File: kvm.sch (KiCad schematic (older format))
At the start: 16 parts, among them J0 USB_C_Receptacle, J1 USB_C_Receptacle, J2 USB_C_Receptacle, U0 HD3SS3212, U1 HD3SS3212, U2 HD3SS3212

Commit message: Added a micro controller and SWD header
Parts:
- removed C?: ?F, symbol Device:C
- removed C? (x2): 1uF, symbol Device:C
- removed D1, D2, D3: D_Schottky, Diode_SMD:D_SOD-123, symbol Device:D_Schottky
- removed R0: 56k, Resistor_SMD:R_0805_2012Metric_Pad1.20x1.40mm_HandSolder, symbol Device:R
- removed R?: 10k, symbol Device:R
- removed U?: MAX17501AxTB, Package_DFN_QFN:TDFN-10-1EP_2x3mm_P0.5mm_EP0.9x2mm, symbol Regulator_Switching:MAX17501AxTB
- added C1, C2: 30p, Capacitor_SMD:C_0805_2012Metric, symbol Device:C
- added J3: Conn_ARM_JTAG_SWD_10, Connector_PinHeader_1.27mm:PinHeader_2x05_P1.27mm_Vertical_SMD, symbol Connector:Conn_ARM_JTAG_SWD_10
- added R2: 10k, Resistor_SMD:R_0805_2012Metric, symbol Device:R
- added SW1: SW_Push, Button_Switch_SMD:SW_SPST_B3S-1000, symbol Switch:SW_Push
- added U3: STM32F030F4Px, Package_SO:TSSOP-20_4.4x6.5mm_P0.65mm, symbol MCU_ST_STM32F0:STM32F030F4Px
- added Y1: Crystal, Crystal:Crystal_HC49-4H_Vertical, symbol Device:Crystal
- J0: footprint Connector_USB:USB_C_Receptacle_GCT_USB4085 -> Connector_USB:USB_C_Receptacle_Amphenol_12401548E4-2A
- J1: renamed from J2; footprint Connector_USB:USB_C_Receptacle_GCT_USB4085 -> Connector_USB:USB_C_Receptacle_Amphenol_12401548E4-2A
- J2: renamed from J1; footprint Connector_USB:USB_C_Receptacle_GCT_USB4085 -> Connector_USB:USB_C_Receptacle_Amphenol_12401548E4-2A
- R1: value 56k -> 10k; footprint Resistor_SMD:R_0805_2012Metric_Pad1.20x1.40mm_HandSolder -> Resistor_SMD:R_0805_2012Metric
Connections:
- net labels added: CRY0, CRY1, I1D+, I1D-, I1RX1+, I1RX1-, I1RX2+, I1RX2-, I1SBU1, I1SBU2, I1TX1+, I1TX1-, I1TX2+, I1TX2-, I2D+, I2D-, I2RX1+, I2RX1-, I2RX2+, I2RX2-, I2SBU1, I2SBU2, I2TX1+, I2TX1-, I2TX2+, I2TX2-, NRST, OD+, OD-, ORX1+, ORX1-, ORX2+, ORX2-, OSBU1, OSBU2, OTX1+, OTX1-, OTX2+, OTX2-, SWCLK, SWDIO
- wire segments 148 -> 126
- no-connect marks 7 -> 15
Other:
- moved on the sheet: J0, J1, J2, U0, U1, U2

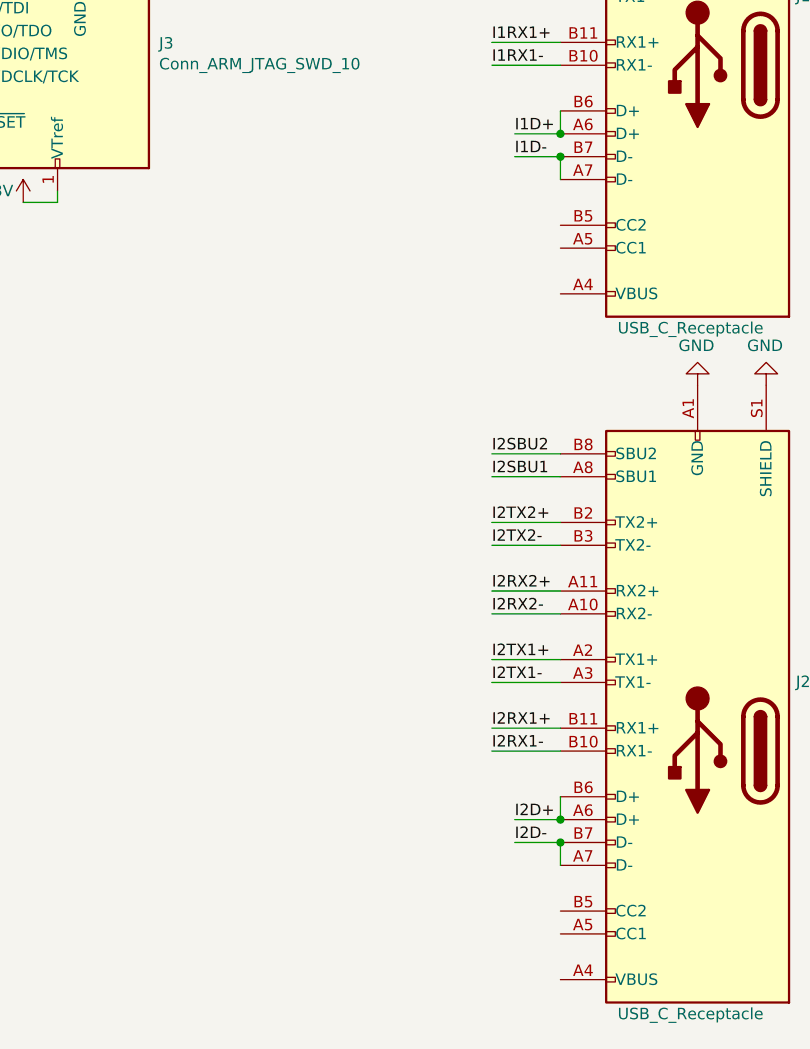
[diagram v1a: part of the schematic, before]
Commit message: Added a power buffer on VBus
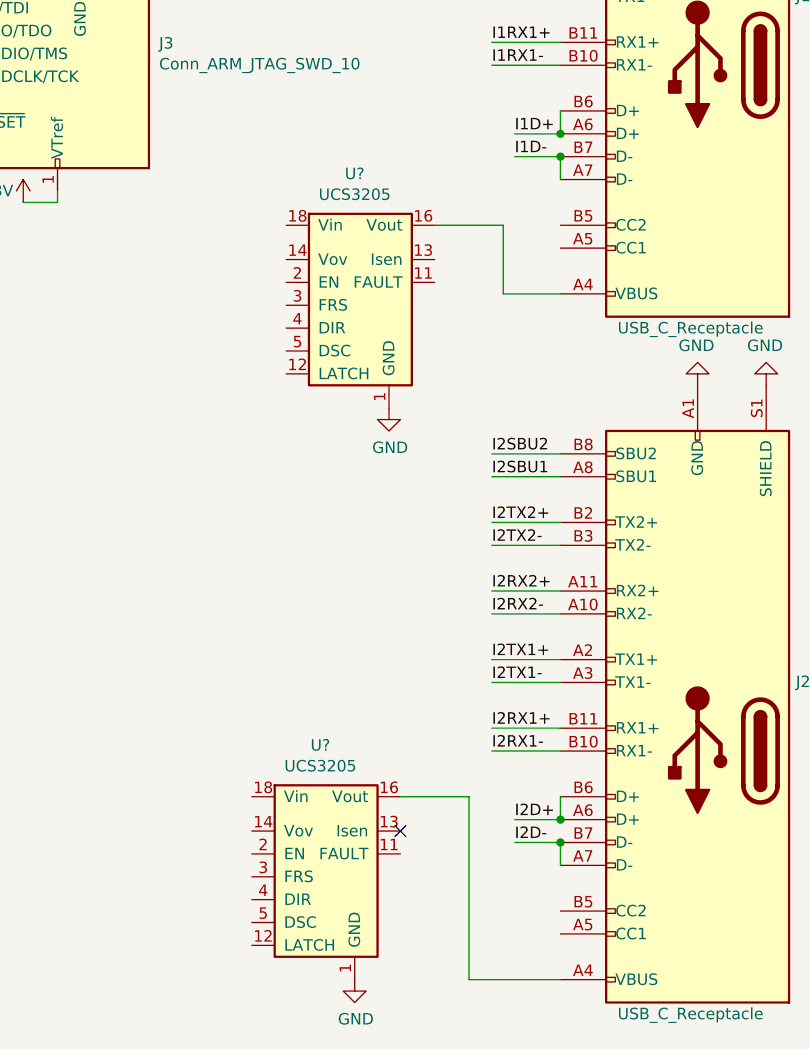
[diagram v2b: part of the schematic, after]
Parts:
- added U? (x2): UCS3205, symbol vendor:UCS3205
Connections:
- net GND: now also U?.1 (GND), U?.1 (GND), U?.15 (GND), U?.15 (GND)
- net at J1.A4 (VBUS), J1.A9 (VBUS), J1.B4 (VBUS)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: now also U?.16 (Vout), U?.17 (Vout), U?.21 (Vout)
- net at J2.A4 (VBUS), J2.A9 (VBUS), J2.B4 (VBUS)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: now also U?.16 (Vout), U?.17 (Vout), U?.21 (Vout)
- new net: U?.18 (Vin), U?.19 (Vin), U?.20 (Vin) (x2)
- no-connect marks 15 -> 16
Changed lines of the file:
@@
 Text Label 5700 2150 0    50   ~ 0
 CRY1
+$Comp
+L vendor:UCS3205 U?
+U 1 1 60CE04F3
+P 9200 3400
+F 0 "U?" H 9200 4025 50  0000 C CNN
+F 1 "UCS3205" H 9200 3934 50  0000 C CNN
+F 2 "" H 9550 3950 50  0001 C CNN
+F 3 "https://www.mouser.co.uk/datasheet/2/268/UCS3205_Data_Sheet_DS20006433A-1915299.pdf" H 9600 3950 50  0001 C CNN
+	1    9200 3400
+	1    0    0    -1
+$EndComp
+$Comp
+L power:GND #PWR?
+U 1 1 60CF5D7A
+P 9350 3800
+F 0 "#PWR?" H 9350 3550 50  0001 C CNN
+F 1 "GND" H 9355 3627 50  0000 C CNN
+F 2 "" H 9350 3800 50  0001 C CNN
+F 3 "" H 9350 3800 50  0001 C CNN
+	1    9350 3800
+	1    0    0    -1
+$EndComp
+Wire Wire Line
+	9550 3000 9850 3000
+Wire Wire Line
+	9850 3000 9850 3300
+Wire Wire Line
+	9850 3300 10100 3300
+$Comp
+L vendor:UCS3205 U?
+U 1 1 60D16145
+P 9050 5900
+F 0 "U?" H 9050 6525 50  0000 C CNN
+F 1 "UCS3205" H 9050 6434 50  0000 C CNN
+F 2 "" H 9400 6450 50  0001 C CNN
+F 3 "https://www.mouser.co.uk/datasheet/2/268/UCS3205_Data_Sheet_DS20006433A-1915299.pdf" H 9450 6450 50  0001 C CNN
+	1    9050 5900
+	1    0    0    -1
+$EndComp
+$Comp
+L power:GND #PWR?
+U 1 1 60D1614B
+P 9200 6300
+F 0 "#PWR?" H 9200 6050 50  0001 C CNN
+F 1 "GND" H 9205 6127 50  0000 C CNN
+F 2 "" H 9200 6300 50  0001 C CNN
+F 3 "" H 9200 6300 50  0001 C CNN
+	1    9200 6300
+	1    0    0    -1
+$EndComp
+Wire Wire Line
+	9400 5500 9700 5500
+Wire Wire Line
+	9700 5500 9700 6300
+Wire Wire Line
+	9700 6300 10100 6300
+NoConn ~ 9400 5650
 $EndSCHEMATC

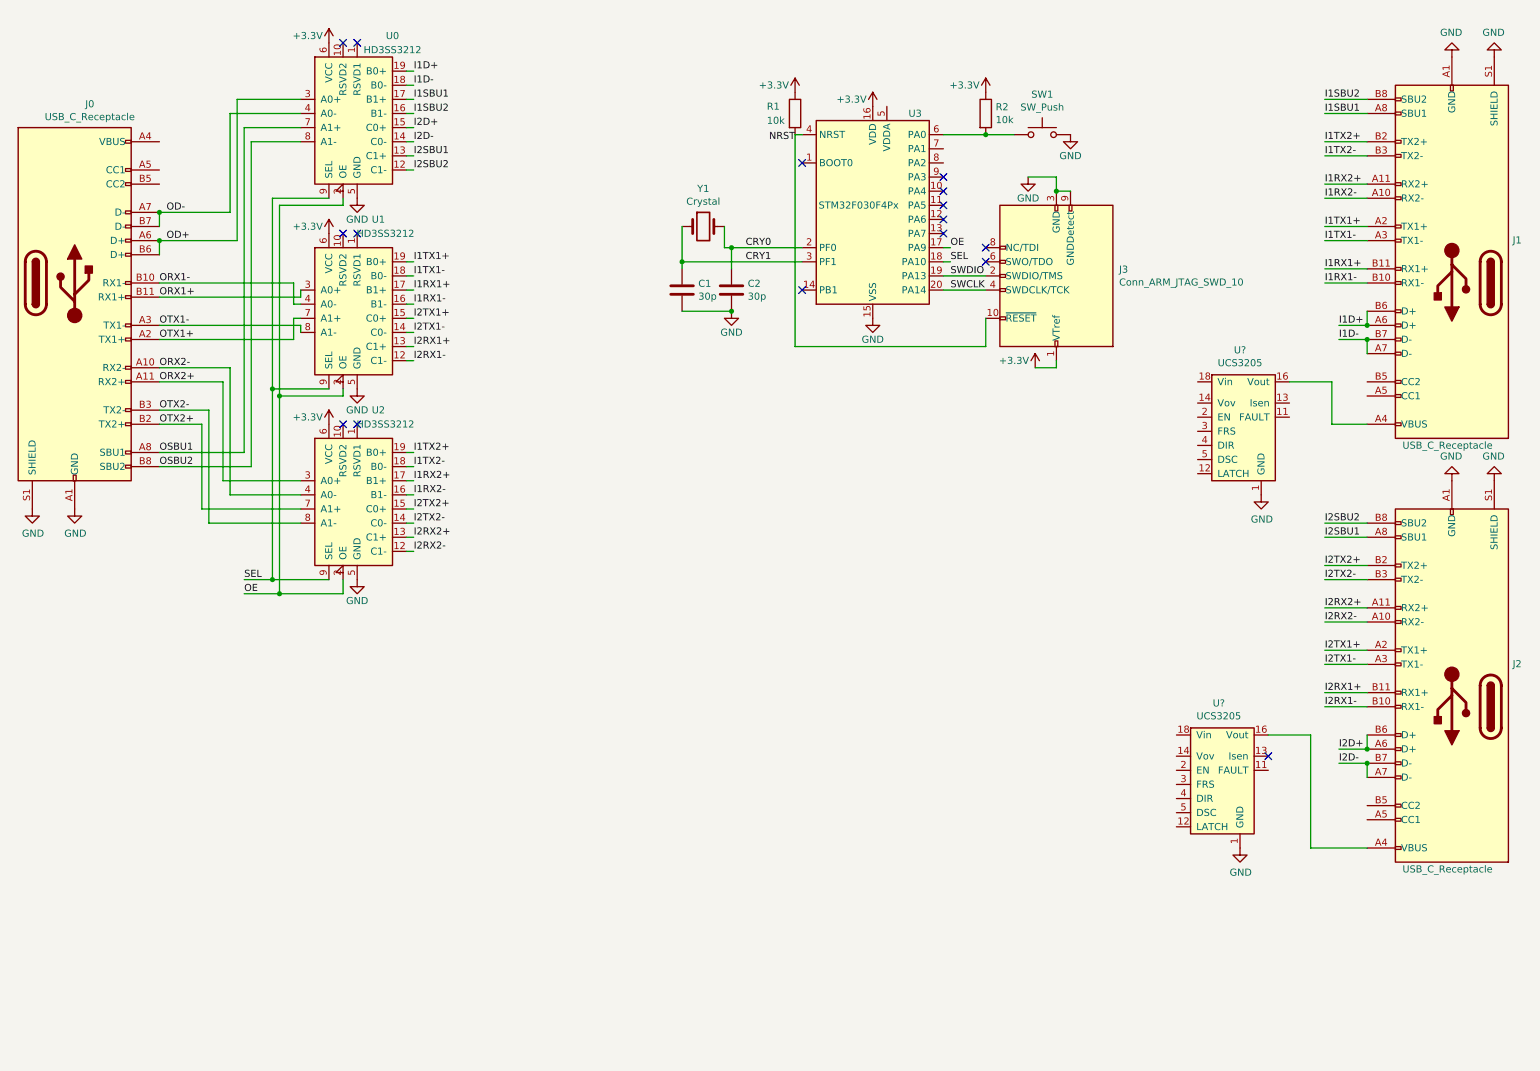
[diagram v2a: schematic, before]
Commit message: finished PD switches and added 3.3V PSU
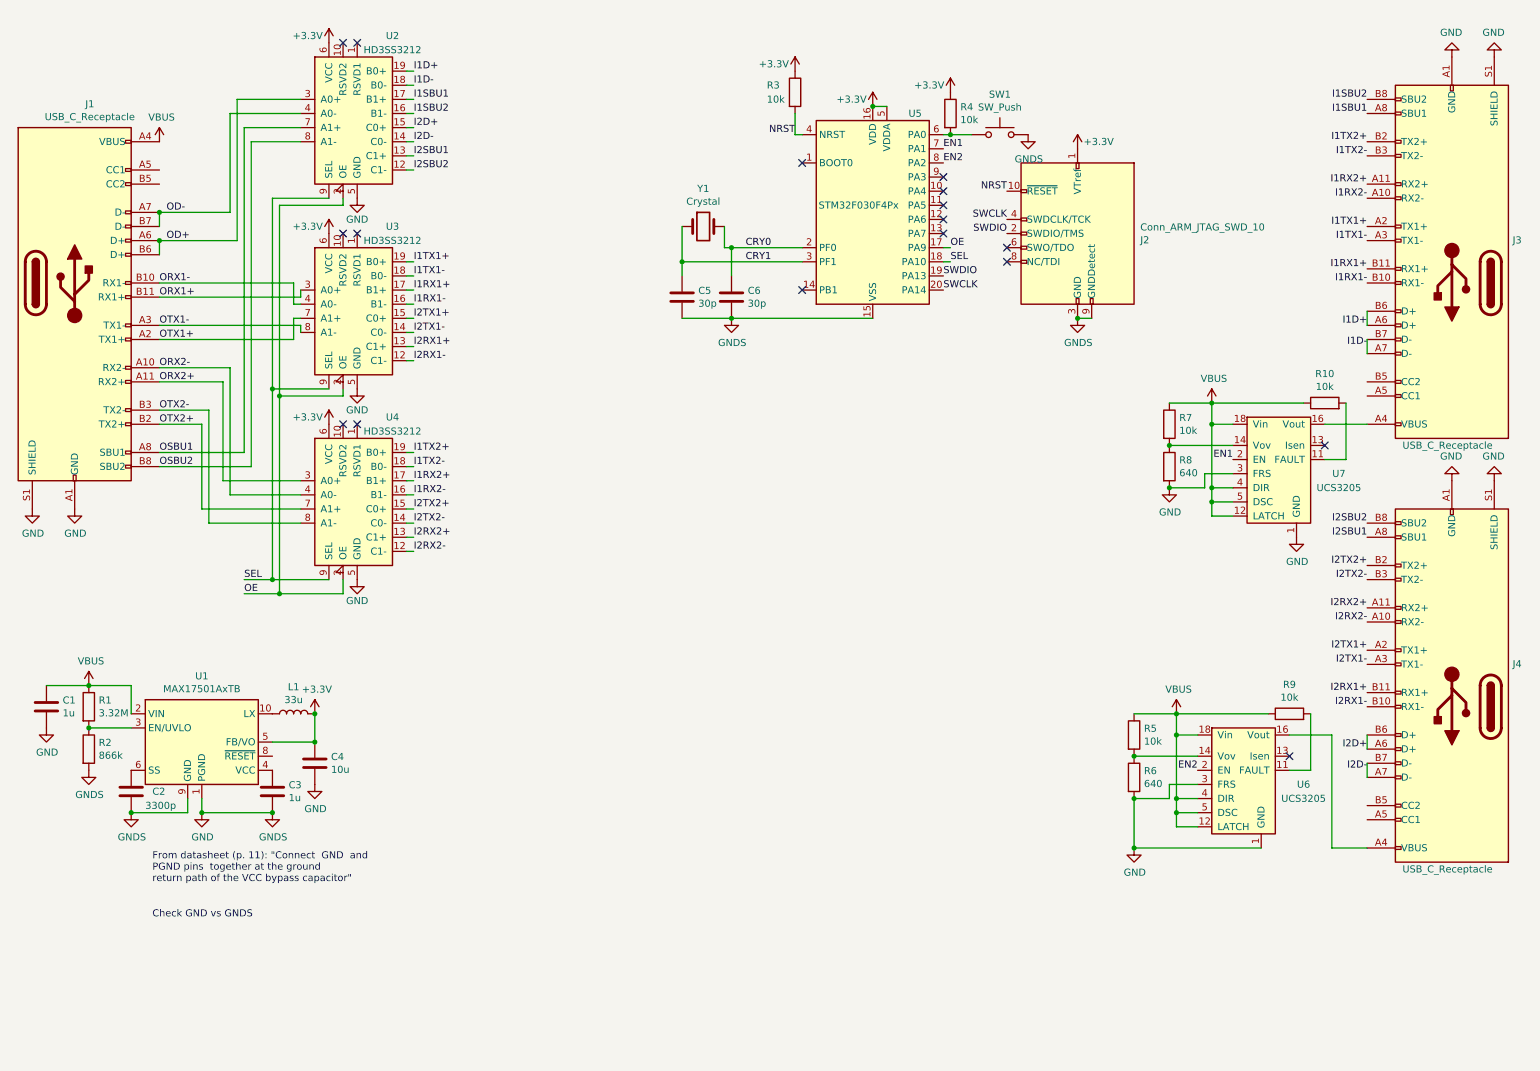
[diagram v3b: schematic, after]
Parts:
- removed U?: UCS3205, symbol vendor:UCS3205
- added C1, C3: 1u, Capacitor_SMD:C_0805_2012Metric, symbol Device:C
- added C2: 3300p, Capacitor_SMD:C_0805_2012Metric, symbol Device:C
- added C4: 10u, Capacitor_SMD:C_1206_3216Metric, symbol Device:C
- added L1: 33u, Inductor_SMD:L_0805_2012Metric, symbol Device:L
- added R1: 3.32M, Resistor_SMD:R_0805_2012Metric, symbol Device:R
- added R10, R5, R7, R9: 10k, Resistor_SMD:R_0805_2012Metric, symbol Device:R
- added R2: 866k, Resistor_SMD:R_0805_2012Metric, symbol Device:R
- added R6, R8: 640, Resistor_SMD:R_0805_2012Metric, symbol Device:R
- added U1: MAX17501AxTB, Package_DFN_QFN:TDFN-10-1EP_2x3mm_P0.5mm_EP0.9x2mm, symbol Regulator_Switching:MAX17501AxTB
- added U7: UCS3205, VQFN20:VQFN19_3x3x0.9mm, symbol vendor:UCS3205
- U6: renamed from U?; footprint (none) -> VQFN20:VQFN19_3x3x0.9mm
- renumbered C1 to C5, C2 to C6, J0 to J1, J3 to J2, J1 to J3, J2 to J4, R1 to R3, R2 to R4, U0 to U2, U1 to U3, U2 to U4, U3 to U5
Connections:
- net +3V3: now also U5.5 (VDDA), C4.1, L1.2, U1.5 (FB/VO)
- net GND: now also U6.3 (FRS), C1.2, C2.2, C3.2, C4.2, R2.2, R6.2, R8.2, U1.1 (PGND), U1.11 (GND), U1.9 (GND), U7.1 (GND), U7.15 (GND), U7.3 (FRS)
- net VBUS: now reaches J1.A4 (VBUS), J1.A9 (VBUS), J1.B4 (VBUS), J1.B9 (VBUS)
- net VBUS: now also U6.12 (LATCH), U6.18 (Vin), U6.19 (Vin), U6.20 (Vin), U6.4 (DIR), U6.5 (DSC), C1.1, R1.1, R10.1, R5.1, R7.1, R9.1, U1.2 (VIN), U7.12 (LATCH), U7.18 (Vin), U7.19 (Vin), U7.20 (Vin), U7.4 (DIR), U7.5 (DSC)
- net at J3.A4 (VBUS), J3.A9 (VBUS), J3.B4 (VBUS)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: now also U7.16 (Vout), U7.17 (Vout), U7.21 (Vout)
- net EN1: now reaches U5.7 (PA1)
- net EN1: now also U7.2 (EN)
- net EN2: now reaches U5.8 (PA2)
- net EN2: now also U6.2 (EN)
- net at U6.11 (FAULT): now also R9.2
- net at U6.14 (Vov): now also R5.2, R6.1
- new net: R10.2, U7.11 (FAULT)
- new net: R7.2, R8.1, U7.14 (Vov)
- new net: L1.1, U1.10 (LX)
- new net: R1.2, R2.1, U1.3 (EN/UVLO)
- new net: C3.1, U1.4 (VCC)
- new net: C2.1, U1.6 (SS)
- no-connect marks 16 -> 17
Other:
- note added: "Check GND vs GNDS"
- note added: "From datasheet (p. 11): "Connect GND and \nPGND pins together at the ground\nreturn path of the VCC bypass capacitor""
- moved on the sheet: C5, C6, J2, R3, R4, SW1, U6

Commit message: Added PD, maybe finished v1!
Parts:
- removed C1, C3: 1u, Capacitor_SMD:C_0805_2012Metric, symbol Device:C
- removed C2: 3300p, Capacitor_SMD:C_0805_2012Metric, symbol Device:C
- removed C4: 10u, Capacitor_SMD:C_1206_3216Metric, symbol Device:C
- removed C5, C6: 30p, Capacitor_SMD:C_0805_2012Metric, symbol Device:C
- removed R1: 3.32M, Resistor_SMD:R_0805_2012Metric, symbol Device:R
- removed R10, R3, R5, R7, R9: 10k, Resistor_SMD:R_0805_2012Metric, symbol Device:R
- removed R2: 866k, Resistor_SMD:R_0805_2012Metric, symbol Device:R
- removed R6, R8: 640, Resistor_SMD:R_0805_2012Metric, symbol Device:R
- removed U6: UCS3205, VQFN20:VQFN19_3x3x0.9mm, symbol vendor:UCS3205
- removed Y1: Crystal, Crystal:Crystal_HC49-4H_Vertical, symbol Device:Crystal
- added C1, C10, C3: 1u, symbol Device:C_Small
- added C2: 3300p, symbol Device:C_Small
- added C4: 10u, symbol Device:C_Small
- added C5, C6: 12p, symbol Device:C_Small
- added C7: 4k7, symbol Device:C_Small
- added C8: 100n, symbol Device:C_Small
- added C9: 10n, symbol Device:C_Small
- added R1: 3M32, symbol Device:R_Small
- added R2: 866k, symbol Device:R_Small
- added R3, R6, R8, R9: 10k, symbol Device:R_Small
- added R5, R7: 640, symbol Device:R_Small
- added U6, U8: TS3A5223RSW, symbol vendor:TS3A5223RSW
- added U9: UCS3205, VQFN20:VQFN19_3x3x0.9mm, symbol vendor:UCS3205
- added Y1: 16MHz, symbol Device:Crystal_GND24_Small
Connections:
- net +3V3: now also C10.1, C4.1, C7.1, C8.1, C9.1, U6.1 (VCC), U8.1 (VCC)
- net EN1: now also U6.4 (SEL1), U6.8 (SEL2)
- net EN2: now also U8.4 (SEL1), U8.8 (SEL2), U9.2 (EN)
- net GND: now also U5.1 (BOOT0), C1.2, C10.2, C2.2, C3.2, C4.2, C5.2, C6.2, C7.2, C8.2, C9.2, R2.2, R5.2, R7.2, U6.6 (GND), U8.6 (GND), U9.1 (GND), U9.15 (GND), U9.3 (FRS), Y1.2, Y1.4
- net VBUS: now also C1.1, R1.1, R3.1, R6.1, R8.1, R9.1, U9.12 (LATCH), U9.18 (Vin), U9.19 (Vin), U9.20 (Vin), U9.4 (DIR), U9.5 (DSC)
- net O_CC1: now reaches J1.A5 (CC1)
- net O_CC1: now also U6.3 (COM1), U8.3 (COM1)
- net O_CC2: now reaches J1.B5 (CC2)
- net O_CC2: now also U6.9 (COM2), U8.9 (COM2)
- net I1_VBUS: now reaches J3.A4 (VBUS), J3.A9 (VBUS), J3.B4 (VBUS), J3.B9 (VBUS), U7.16 (Vout), U7.17 (Vout), U7.21 (Vout)
- net I1_CC1: now reaches J3.A5 (CC1)
- net I1_CC1: now also U6.2 (NO1)
- net I1_CC2: now reaches J3.B5 (CC2)
- net I1_CC2: now also U6.10 (NO2)
- net I2_VBUS: now reaches J4.A4 (VBUS), J4.A9 (VBUS), J4.B4 (VBUS), J4.B9 (VBUS)
- net I2_VBUS: now also U9.16 (Vout), U9.17 (Vout), U9.21 (Vout)
- net I2_CC1: now reaches J4.A5 (CC1)
- net I2_CC1: now also U8.2 (NO1)
- net I2_CC2: now reaches J4.B5 (CC2)
- net I2_CC2: now also U8.10 (NO2)
- net at U7.11 (FAULT): now also R8.2
- net at U7.14 (Vov): now also R3.2, R5.1
- net at U1.3 (EN/UVLO): now also R1.2, R2.1
- net at U1.4 (VCC): now also C3.1
- net at U1.6 (SS): now also C2.1
- net CRY0: no longer names the net of U5.2 (PF0)
- net CRY0: now also C6.1, Y1.3
- net CRY1: no longer names the net of U5.3 (PF1)
- net CRY1: now also C5.1, Y1.1
- net I1D+ renamed I1_D+
- net I1D- renamed I1_D-
- net I1RX1+ renamed I1_RX1+
- net I1RX1- renamed I1_RX1-
- net I1RX2+ renamed I1_RX2+
- net I1RX2- renamed I1_RX2-
- net I1SBU1 renamed I1_SBU1
- net I1SBU2 renamed I1_SBU2
- net I1TX1+ renamed I1_TX1+
- net I1TX1- renamed I1_TX1-
- net I1TX2+ renamed I1_TX2+
- net I1TX2- renamed I1_TX2-
- net I2D+ renamed I2_D+
- net I2D- renamed I2_D-
- net I2RX1+ renamed I2_RX1+
- net I2RX1- renamed I2_RX1-
- net I2RX2+ renamed I2_RX2+
- net I2RX2- renamed I2_RX2-
- net I2SBU1 renamed I2_SBU1
- net I2SBU2 renamed I2_SBU2
- net I2TX1+ renamed I2_TX1+
- net I2TX1- renamed I2_TX1-
- net I2TX2+ renamed I2_TX2+
- net I2TX2- renamed I2_TX2-
- net OD+ renamed O_D+
- net OD- renamed O_D-
- net ORX1+ renamed O_RX1+
- net ORX1- renamed O_RX1-
- net ORX2+ renamed O_RX2+
- net ORX2- renamed O_RX2-
- net OSBU1 renamed O_SBU1
- net OSBU2 renamed O_SBU2
- net OTX1+ renamed O_TX1+
- net OTX1- renamed O_TX1-
- net OTX2+ renamed O_TX2+
- net OTX2- renamed O_TX2-
- new net: R9.2, U9.11 (FAULT)
- new net: R6.2, R7.1, U9.14 (Vov)
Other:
- note added: "3V3 PSU"
- note added: "Check GND and GNDS"
- note added: "Input 1"
- note added: "Input 2"
- note added: "MCU"
- note added: "Output"
- note added: "Power Delivery"
- note added: "Switching"
- note removed: "Check GND vs GNDS"
- moved on the sheet: J2, L1, R4, SW1, U1, U2, U3, U4, U5, U7
